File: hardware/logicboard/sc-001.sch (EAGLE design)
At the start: 10 parts

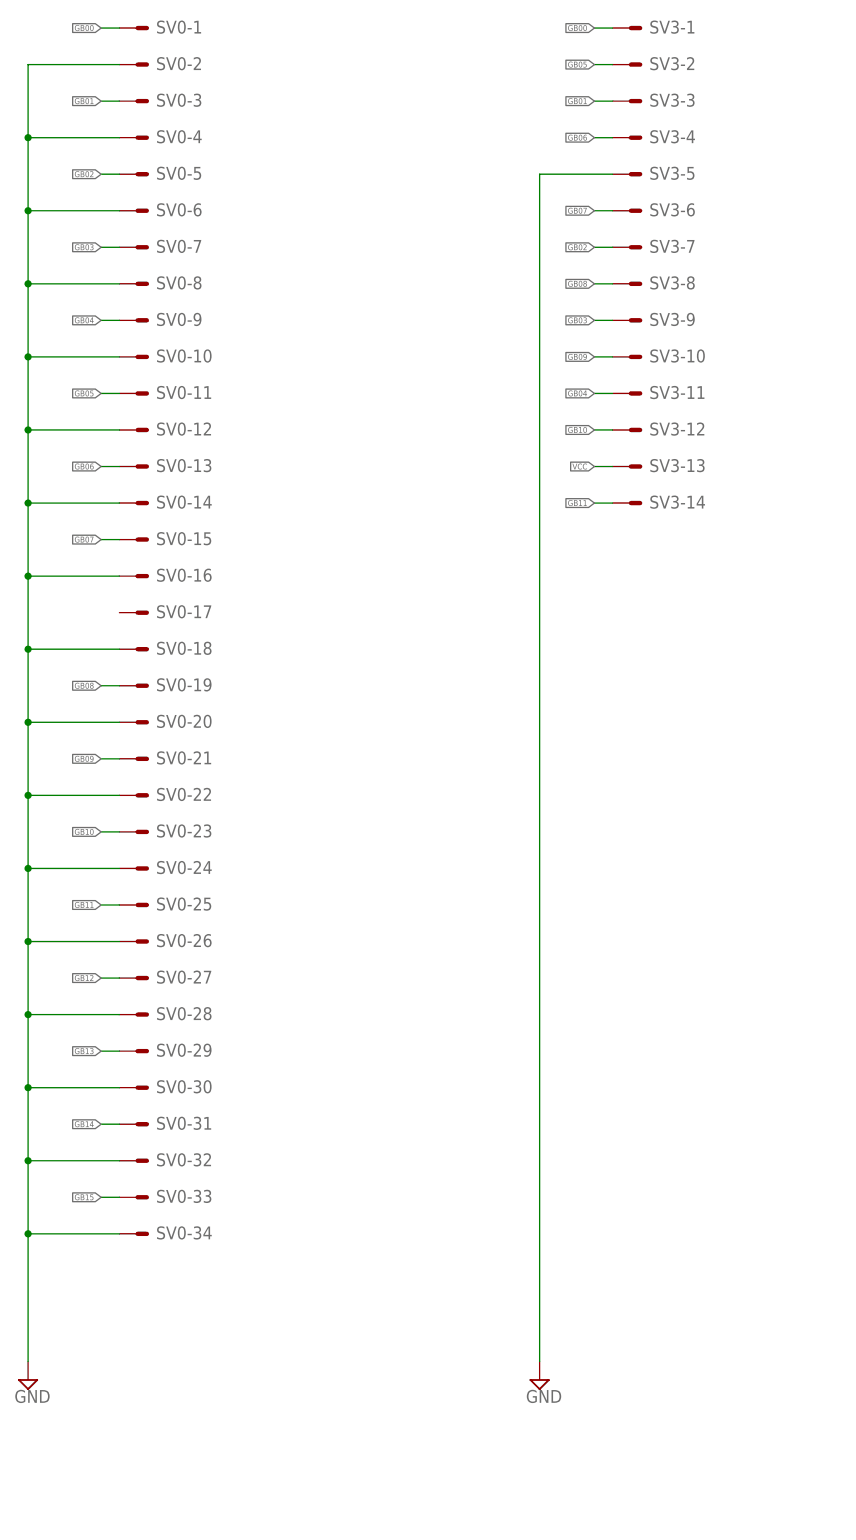
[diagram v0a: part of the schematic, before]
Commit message: Changed board size.
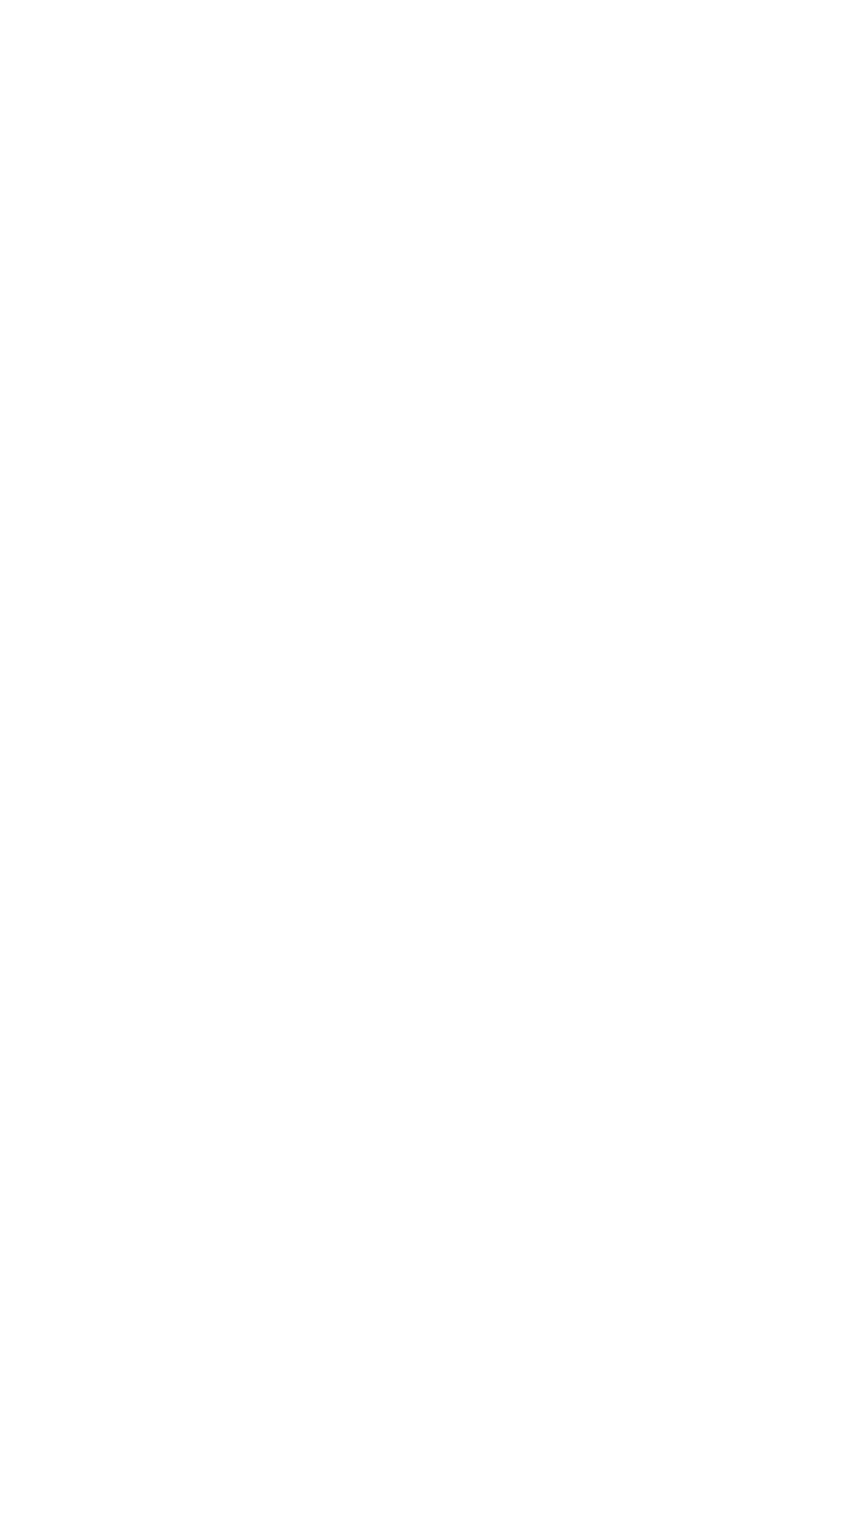
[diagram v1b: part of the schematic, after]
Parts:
- removed SV0: (no value), con-ml:ML34LE
- removed SV3: (no value), con-ml:ML14LE
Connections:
- removed net GB00: SV0-1.S, SV3-1.S
- removed net GB01: SV0-3.S, SV3-3.S
- removed net GB02: SV0-5.S, SV3-7.S
- removed net GB03: SV0-7.S, SV3-9.S
- removed net GB04: SV0-9.S, SV3-11.S
- removed net GB05: SV0-11.S, SV3-2.S
- removed net GB06: SV0-13.S, SV3-4.S
- removed net GB07: SV0-15.S, SV3-6.S
- removed net GB08: SV0-19.S, SV3-8.S
- removed net GB09: SV0-21.S, SV3-10.S
- removed net GB10: SV0-23.S, SV3-12.S
- removed net GB11: SV0-25.S, SV3-14.S
- net GB12: no longer SV0-27.S
- net GB13: no longer SV0-29.S
- net GB14: no longer SV0-31.S
- net GB15: no longer SV0-33.S
- net GND: no longer SV0-10.S, SV0-12.S, SV0-14.S, SV0-16.S, SV0-18.S, SV0-2.S, SV0-20.S, SV0-22.S, SV0-24.S, SV0-26.S, SV0-28.S, SV0-30.S, SV0-32.S, SV0-34.S, SV0-4.S, SV0-6.S, SV0-8.S, SV3-5.S
- net VCC: no longer SV3-13.S

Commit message: Added parts.
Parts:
- added D1, D2, D3, D4: 200mA/100V/1V, SparkFun-DiscreteSemi:DIODE-1N4148
- added Q1, Q2, Q3, Q4: 60V/32A/35mΩ, SparkFun-DiscreteSemi:MOSFET-NCH-FQP30N06L
- added SV2: (no value), con-ml:ML16LE
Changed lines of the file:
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@@
 <part name="SUPPLY5" library="supply2" library_urn="urn:adsk.eagle:library:372" deviceset="GND" device=""/>
 <part name="SUPPLY6" library="supply2" library_urn="urn:adsk.eagle:library:372" deviceset="GND" device=""/>
+<part name="Q1" library="SparkFun-DiscreteSemi" library_urn="urn:adsk.eagle:library:514" deviceset="MOSFET-NCH" device="-FQP30N06L" package3d_urn="urn:adsk.eagle:package:38447/1" value="60V/32A/35mΩ"/>
+<part name="Q2" library="SparkFun-DiscreteSemi" library_urn="urn:adsk.eagle:library:514" deviceset="MOSFET-NCH" device="-FQP30N06L" package3d_urn="urn:adsk.eagle:package:38447/1" value="60V/32A/35mΩ"/>
+<part name="Q3" library="SparkFun-DiscreteSemi" library_urn="urn:adsk.eagle:library:514" deviceset="MOSFET-NCH" device="-FQP30N06L" package3d_urn="urn:adsk.eagle:package:38447/1" value="60V/32A/35mΩ"/>
+<part name="Q4" library="SparkFun-DiscreteSemi" library_urn="urn:adsk.eagle:library:514" deviceset="MOSFET-NCH" device="-FQP30N06L" package3d_urn="urn:adsk.eagle:package:38447/1" value="60V/32A/35mΩ"/>
+<part name="D1" library="SparkFun-DiscreteSemi" library_urn="urn:adsk.eagle:library:514" deviceset="DIODE" device="-1N4148" package3d_urn="urn:adsk.eagle:package:38452/1" value="200mA/100V/1V"/>
+<part name="D2" library="SparkFun-DiscreteSemi" library_urn="urn:adsk.eagle:library:514" deviceset="DIODE" device="-1N4148" package3d_urn="urn:adsk.eagle:package:38452/1" value="200mA/100V/1V"/>
+<part name="D3" library="SparkFun-DiscreteSemi" library_urn="urn:adsk.eagle:library:514" deviceset="DIODE" device="-1N4148" package3d_urn="urn:adsk.eagle:package:38452/1" value="200mA/100V/1V"/>
+<part name="D4" library="SparkFun-DiscreteSemi" library_urn="urn:adsk.eagle:library:514" deviceset="DIODE" device="-1N4148" package3d_urn="urn:adsk.eagle:package:38452/1" value="200mA/100V/1V"/>
+<part name="SV2" library="con-ml" library_urn="urn:adsk.eagle:library:164" deviceset="ML16LE" device="" package3d_urn="urn:adsk.eagle:package:8682/1"/>
 </parts>
 <sheets>
@@
 <attribute name="VALUE" x="221.615" y="52.705" size="1.778" layer="96"/>
 </instance>
+<instance part="Q1" gate="NMOS" x="203.2" y="236.22" smashed="yes">
+<attribute name="NAME" x="208.28" y="236.22" size="1.778" layer="95" font="vector"/>
+<attribute name="VALUE" x="208.28" y="233.68" size="1.778" layer="96" font="vector"/>
+</instance>
+<instance part="Q2" gate="NMOS" x="203.2" y="213.36" smashed="yes">
+<attribute name="NAME" x="208.28" y="213.36" size="1.778" layer="95" font="vector"/>
+<attribute name="VALUE" x="208.28" y="210.82" size="1.778" layer="96" font="vector"/>
+</instance>
+<instance part="Q3" gate="NMOS" x="203.2" y="193.04" smashed="yes">
+<attribute name="NAME" x="208.28" y="193.04" size="1.778" layer="95" font="vector"/>
+<attribute name="VALUE" x="208.28" y="190.5" size="1.778" layer="96" font="vector"/>
+</instance>
+<instance part="Q4" gate="NMOS" x="203.2" y="172.72" smashed="yes">
+<attribute name="NAME" x="208.28" y="172.72" size="1.778" layer="95" font="vector"/>
+<attribute name="VALUE" x="208.28" y="170.18" size="1.778" layer="96" font="vector"/>
+</instance>
+<instance part="D1" gate="G$1" x="246.38" y="236.22" smashed="yes">
+<attribute name="NAME" x="243.84" y="238.252" size="1.778" layer="95" font="vector"/>
+<attribute name="VALUE" x="243.84" y="234.188" size="1.778" layer="96" font="vector" align="top-left"/>
+</instance>
+<instance part="D2" gate="G$1" x="248.92" y="218.44" smashed="yes">
+<attribute name="NAME" x="246.38" y="220.472" size="1.778" layer="95" font="vector"/>
+<attribute name="VALUE" x="246.38" y="216.408" size="1.778" layer="96" font="vector" align="top-left"/>
+</instance>
+<instance part="D3" gate="G$1" x="246.38" y="195.58" smashed="yes">
+<attribute name="NAME" x="243.84" y="197.612" size="1.778" layer="95" font="vector"/>
+<attribute name="VALUE" x="243.84" y="193.548" size="1.778" layer="96" font="vector" align="top-left"/>
+</instance>
+<instance part="D4" gate="G$1" x="246.38" y="172.72" smashed="yes">
+<attribute name="NAME" x="243.84" y="174.752" size="1.778" layer="95" font="vector"/>
+<attribute name="VALUE" x="243.84" y="170.688" size="1.778" layer="96" font="vector" align="top-left"/>
+</instance>
+<instance part="SV2" gate="-1" x="83.82" y="241.3" smashed="yes">
+<attribute name="NAME" x="86.36" y="240.538" size="1.778" layer="95"/>
+<attribute name="VALUE" x="83.566" y="238.379" size="1.778" layer="96"/>
+</instance>
+<instance part="SV2" gate="-2" x="83.82" y="236.22" smashed="yes">
+<attribute name="NAME" x="86.36" y="235.458" size="1.778" layer="95"/>
+<attribute name="VALUE" x="83.566" y="233.299" size="1.778" layer="96"/>
+</instance>
+<instance part="SV2" gate="-3" x="83.82" y="231.14" smashed="yes">
+<attribute name="NAME" x="86.36" y="230.378" size="1.778" layer="95"/>
+<attribute name="VALUE" x="83.566" y="228.219" size="1.778" layer="96"/>
+</instance>
+<instance part="SV2" gate="-4" x="83.82" y="226.06" smashed="yes">
+<attribute name="NAME" x="86.36" y="225.298" size="1.778" layer="95"/>
+<attribute name="VALUE" x="83.566" y="223.139" size="1.778" layer="96"/>
+</instance>
+<instance part="SV2" gate="-5" x="83.82" y="220.98" smashed="yes">
+<attribute name="NAME" x="86.36" y="220.218" size="1.778" layer="95"/>
+<attribute name="VALUE" x="83.566" y="218.059" size="1.778" layer="96"/>
+</instance>
+<instance part="SV2" gate="-6" x="83.82" y="215.9" smashed="yes">
+<attribute name="NAME" x="86.36" y="215.138" size="1.778" layer="95"/>
+<attribute name="VALUE" x="83.566" y="212.979" size="1.778" layer="96"/>
+</instance>
+<instance part="SV2" gate="-7" x="83.82" y="210.82" smashed="yes">
+<attribute name="NAME" x="86.36" y="210.058" size="1.778" layer="95"/>
+<attribute name="VALUE" x="83.566" y="207.899" size="1.778" layer="96"/>
+</instance>
+<instance part="SV2" gate="-8" x="83.82" y="205.74" smashed="yes">
+<attribute name="NAME" x="86.36" y="204.978" size="1.778" layer="95"/>
+<attribute name="VALUE" x="83.566" y="202.819" size="1.778" layer="96"/>
+</instance>
+<instance part="SV2" gate="-9" x="104.14" y="241.3" smashed="yes">
+<attribute name="NAME" x="106.68" y="240.538" size="1.778" layer="95"/>
+<attribute name="VALUE" x="103.886" y="238.379" size="1.778" layer="96"/>
+</instance>
+<instance part="SV2" gate="-10" x="104.14" y="236.22" smashed="yes">
+<attribute name="NAME" x="106.68" y="235.458" size="1.778" layer="95"/>
+<attribute name="VALUE" x="103.886" y="233.299" size="1.778" layer="96"/>
+</instance>
+<instance part="SV2" gate="-11" x="104.14" y="231.14" smashed="yes">
+<attribute name="NAME" x="106.68" y="230.378" size="1.778" layer="95"/>
+<attribute name="VALUE" x="103.886" y="228.219" size="1.778" layer="96"/>
+</instance>
+<instance part="SV2" gate="-12" x="104.14" y="226.06" smashed="yes">
+<attribute name="NAME" x="106.68" y="225.298" size="1.778" layer="95"/>
+<attribute name="VALUE" x="103.886" y="223.139" size="1.778" layer="96"/>
+</instance>
+<instance part="SV2" gate="-13" x="104.14" y="220.98" smashed="yes">
+<attribute name="NAME" x="106.68" y="220.218" size="1.778" layer="95"/>
+<attribute name="VALUE" x="103.886" y="218.059" size="1.778" layer="96"/>
+</instance>
+<instance part="SV2" gate="-14" x="104.14" y="215.9" smashed="yes">
+<attribute name="NAME" x="106.68" y="215.138" size="1.778" layer="95"/>
+<attribute name="VALUE" x="103.886" y="212.979" size="1.778" layer="96"/>
+</instance>
+<instance part="SV2" gate="-15" x="104.14" y="210.82" smashed="yes">
+<attribute name="NAME" x="106.68" y="210.058" size="1.778" layer="95"/>
+<attribute name="VALUE" x="103.886" y="207.899" size="1.778" layer="96"/>
+</instance>
+<instance part="SV2" gate="-16" x="104.14" y="205.74" smashed="yes">
+<attribute name="NAME" x="106.68" y="204.978" size="1.778" layer="95"/>
+<attribute name="VALUE" x="103.886" y="202.819" size="1.778" layer="96"/>
+</instance>
 </instances>

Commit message: Schematic.
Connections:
- removed net GB12: SV1-2.S
- removed net GB13: SV1-6.S
- removed net GB14: SV1-10.S
- removed net GB15: SV1-14.S
- new net ANLG0: SV1-3.S
- new net ANLG1: SV1-7.S
- new net ANLG2: SV1-11.S
- new net ANLG3: SV1-15.S
- new net DRVR0: D1.A, Q1.D
- new net DRVR1: D2.A, Q2.D
- new net DRVR2: D3.A, Q3.D
- new net DRVR3: D4.A, Q4.D
- new net DTCT0: Q1.G, SV1-2.S
- new net DTCT1: Q2.G, SV1-6.S
- new net DTCT2: Q3.G, SV1-10.S
- new net DTCT3: Q4.G, SV1-14.S
- net GND: now also Q1.S, Q2.S, Q3.S, Q4.S
- net VCC/2: now also D1.C, D2.C, D3.C, D4.C
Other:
- moved on the sheet: D1, D2, D3, D4, Q1, Q2, Q3, Q4

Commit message: Routed.
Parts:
- removed C2: (no value), rcl:C-EU025-025X050
- removed LED2: (no value), led:LED3MM
- removed R2: 1k, rcl:R-EU_0204/5
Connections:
- removed net VCC: C1.1, R1.1
- removed net VCCLED: LED1.A, R1.2
- net ANLG0: now also SV2-3.S
- net ANLG1: now also SV2-7.S
- net ANLG2: now also SV2-11.S
- net ANLG3: now also SV2-15.S
- net DRVR0: now also SV2-2.S
- net DRVR1: now also SV2-6.S
- net DRVR2: now also SV2-10.S
- net DRVR3: now also SV2-14.S
- net GND: now also SV2-1.S, SV2-13.S, SV2-5.S, SV2-9.S; no longer C2.2, LED2.C
- net VCC/2: now also C1.1, R1.1, SV2-12.S, SV2-16.S, SV2-4.S, SV2-8.S; no longer C2.1, R2.1
- net VCC2LED: now also LED1.A, R1.2; no longer LED2.A, R2.2
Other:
- moved on the sheet: C1, LED1, R1, SV2-1, SV2-10, SV2-11, SV2-12, SV2-13, SV2-14, SV2-15, SV2-16, SV2-2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
